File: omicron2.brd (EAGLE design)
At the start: 76.2 x 53.3 mm, 180 parts, among them IC1 XC6SLX4-2TQG144, IC2 TPS73033DBV, IC3 LD6806TD/12H, IC4 MT48LC64M4A2, IC5 M25P40-2253716, IC6 TPS73033DBV, X1 USB-MICRO-B-BOTTOM, X2 7C-33.3-1842039

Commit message: backup
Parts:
- removed C31, C32: (no value), rcl:C0603
- TP13, TP14, TP15, TP16: value TPTP15R -> TPTP20R; device testpad:TP15R -> testpad:TP20R
- moved TP10 55.7 mm to (71.1, 34.9), turned to 180 degrees
- moved C6 52.3 mm to (40.6, 50.2), turned to 270 degrees
- moved C2 48.0 mm to (40.6, 46.4)
- moved IC2 47.4 mm to (43.2, 48.3), turned to 180 degrees
- moved IC3 46.0 mm to (50.2, 48.3), turned to 180 degrees
- moved C1 44.5 mm to (45.7, 46.4), turned to 90 degrees
- moved C5 43.9 mm to (47.6, 46.4), turned to 90 degrees
- moved L3 41.8 mm to (41.3, 41.3)
- moved TP9 41.2 mm to (43.2, 43.8), turned to 0 degrees
- moved C33 39.9 mm to (36.8, 43.8), turned to 270 degrees
- moved X2 39.0 mm to (33.7, 43.8), turned to 270 degrees
- moved TP8 38.6 mm to (47.6, 43.8), turned to 0 degrees
- moved L2 34.6 mm to (43.2, 41.3), turned to 270 degrees
- moved L1 33.3 mm to (45.1, 41.3), turned to 270 degrees
- moved TP14 30.2 mm to (73.7, 49.5)
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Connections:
- net CLK_33: now also IC1.134; no longer IC1.51
- net GND: no longer C31.2, C32.2
- net LED1: now also IC1.48
- net LED2: now also IC1.47
- net LED3: now also IC1.46
- net M_A4: now also IC1.132; no longer IC1.101
- net M_PWREN: now also IC1.101
- net USB_D+: now also IC1.59; no longer C32.1, IC1.61
- net USB_D-: no longer C31.1
- net USB_PUP: now also IC1.67; no longer IC1.59
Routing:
- net +5V: track 26.3 -> 172.9 mm, vias 1 -> 3
- net GND: track 550.4 -> 671.7 mm, vias 50 -> 45
- net VCC_MEM: track 0.00 -> 50.4 mm, vias 0 -> 2
- net USB_S-: track 10.9 -> 52.2 mm, vias 0 -> 1
- net USB_S+: track 13.8 -> 52.1 mm, vias 0 -> 1
- net TDI: track 0.00 -> 35.8 mm, vias 0 -> 2
- net TCK: track 0.00 -> 34.7 mm, vias 0 -> 2
- net TMS: track 0.00 -> 31.6 mm, vias 0 -> 2
- net TDO: track 0.00 -> 30.8 mm, vias 0 -> 2
- net M_PWREN: track 0.00 -> 25.3 mm, vias 0 -> 1
- net M_A4: track 31.0 -> 52.1 mm
- net +3V3: track 220.3 -> 241.2 mm, vias 12 -> 14
- net CFG_DONE: track 2.17 -> 17.7 mm, vias 0 -> 2
- net FLASH_SO: track 23.9 -> 8.38 mm
- net LED1: track 0.00 -> 11.3 mm
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- added copper zone on layer 1, net GND
- added copper zone on layer 16, net GND
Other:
- board text added: "TCK"
- board text added: "TDI"
- board text added: "TMS"
- board text added: "omicron"
- board text added: "v2.0"

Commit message: backup
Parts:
- added C31, C32: 470nF, rcl:C0603
- added Q1, Q3: (no value), transistors:SOT323
- added Q2, Q4: BC807W, transistor-pnp:SOT323-BEC
- added R60, R61: 6k8 1%, rcl:R0603
- TP2: value TPTP15R -> TPTP20R; device testpad:TP15R -> testpad:TP20R
- moved TP2 54.9 mm to (73.7, 39.4)
- moved TP1 3.24 mm to (24.1, 12.1)
- moved C27 0.64 mm to (23.8, 28.3)
- moved C37 0.63 mm to (62.9, 34.9)
- moved L1 0.63 mm to (44.5, 41.3)
- moved L2 0.63 mm to (42.5, 41.3)
- moved L3 0.63 mm to (40.6, 41.3)
- moved TP3 0.63 mm to (60.3, 34.9)
- moved TP9 0.63 mm to (42.5, 43.8)
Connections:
- new net N$24: Q1.3, R60.2
- new net N$25: Q4.1, R61.1
- new net N$26: Q3.3, R61.2
- new net N$7: Q2.1, R60.1
- new net VIO33: IC1.44, Q3.1
- new net VIO50: IC1.45, Q1.1
- net +3V3: now also C31.1, C32.1, Q4.2
- net +5V: now also Q2.2
- net GND: now also C31.2, C32.2, Q1.2, Q3.2
- net S10: now also IC1.23; no longer IC1.24
- net S11: now also IC1.26; no longer IC1.27
- net S12: now also IC1.29; no longer IC1.30
- net S13: now also IC1.32; no longer IC1.33
- net S14: now also IC1.34; no longer IC1.39
- net S15: now also IC1.39; no longer IC1.41
- net S16: now also IC1.41; no longer IC1.44
- net S9: now also IC1.21; no longer IC1.22
- net SD10: now also IC1.24; no longer IC1.26
- net SD11: now also IC1.27; no longer IC1.29
- net SD12: now also IC1.30; no longer IC1.32
- net SD13: now also IC1.33; no longer IC1.34
- net SD14: now also IC1.35; no longer IC1.40
- net SD15: now also IC1.40; no longer IC1.43
- net SD16: now also IC1.43; no longer IC1.45
- net SD9: now also IC1.22; no longer IC1.23
- net VCC_B2: now also Q2.3, Q4.3
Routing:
- net VCC_B2: track 44.9 -> 60.3 mm, vias 1 -> 2
- net GND: track 671.7 -> 686.8 mm, vias 45 -> 44
- net VIO33: track 0.00 -> 14.5 mm, vias 0 -> 1
- net VIO50: track 0.00 -> 14.2 mm, vias 0 -> 1
- net +3V3: track 241.2 -> 253.4 mm, vias 14 -> 15
- net N$26: track 0.00 -> 3.77 mm
- net SD15: track 31.0 -> 28.2 mm
- net S16: track 25.8 -> 23.0 mm
- net +5V: track 172.9 -> 175.7 mm
- net SD16: track 35.1 -> 32.5 mm
- net SD14: track 26.5 -> 23.9 mm
- net N$24: track 0.00 -> 2.23 mm
- net S14: track 18.1 -> 16.2 mm
- net N$7: track 0.00 -> 1.82 mm
- net RESET_N: track 5.82 -> 7.61 mm
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- removed copper zone on layer 1, net GND
- removed copper zone on layer 16, net GND

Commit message: Initial commit.
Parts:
- added C38, C39: 470nF, rcl:C0603
- added C40: 2.2uF, rcl:C0603
- added R62, R63: 68, rcl:R0603
- added U$1: PIC10F320, pic10f320:SOT23
- moved LED1 48.4 mm to (26.0, 50.2), flipped to the bottom, turned to 0 degrees
- moved LED2 47.9 mm to (27.9, 50.2), flipped to the bottom, turned to 0 degrees
- moved LED4 47.9 mm to (31.8, 50.2), flipped to the bottom, turned to 0 degrees
- moved LED3 47.6 mm to (29.8, 50.2), flipped to the bottom, turned to 0 degrees
- moved R4 42.2 mm to (26.0, 47.0), flipped to the bottom, turned to 90 degrees
- moved R10 42.0 mm to (34.3, 47.6), flipped to the bottom, turned to 0 degrees
- moved R8 41.6 mm to (27.9, 47.0), flipped to the bottom, turned to 90 degrees
- moved R9 41.3 mm to (29.8, 47.0), flipped to the bottom, turned to 90 degrees
- moved LED5 15.4 mm to (46.4, 15.9), turned to 90 degrees
- moved R59 11.2 mm to (46.4, 14.0), turned to 0 degrees
- moved C4 8.82 mm to (37.5, 22.9), turned to 90 degrees
- moved C9 8.09 mm to (39.7, 26.0), turned to 0 degrees
- moved Q2 3.18 mm to (21.0, 2.54)
- moved Q4 3.18 mm to (18.4, 2.54)
- moved R60 2.54 mm to (22.2, 5.08)
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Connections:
- new net AD_RA0: IC1.46, U$1.1
- new net AD_RA1: IC1.47, U$1.3
- new net AD_RA3: IC1.51, U$1.6
- new net N$27: C39.1, R62.2, R63.2, U$1.4
- net +3V3: now also C38.1, U$1.5
- net +5V: now also C40.1
- net GND: now also C38.2, C39.2, C40.2, R62.1, U$1.2
- net LED1: now also IC1.139; no longer IC1.48
- net LED2: now also IC1.138; no longer IC1.47
- net LED3: now also IC1.133; no longer IC1.46
- net VCC_B2: now also R63.1
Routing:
- net N$27: track 0.00 -> 14.4 mm
- net CFG_DONE: track 17.7 -> 4.49 mm, vias 2 -> 0
- net AD_RA1: track 0.00 -> 12.8 mm
- net AD_RA3: track 0.00 -> 9.72 mm
- net AD_RA0: track 0.00 -> 9.60 mm
- net +3V3: track 253.4 -> 260.7 mm
- net GND: track 686.8 -> 690.4 mm, vias 44 -> 45
- net VCC_B2: track 60.3 -> 63.8 mm
- net N$25: track 1.67 -> 4.62 mm
- net N$4: track 1.58 -> 4.12 mm
- net N$26: track 3.77 -> 1.43 mm
- net LED2: track 10.7 -> 8.55 mm, vias 0 -> 1
- net LED1: track 11.3 -> 9.13 mm, vias 0 -> 1
- net N$91: track 1.58 -> 3.48 mm
- net +5V: track 175.7 -> 177.2 mm
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- added copper zone on layer 1, net GND
- added copper zone on layer 16, net GND

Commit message: Final touches.
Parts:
- added C41, C42, C43: 470nF, rcl:C0603
- moved TP9 0.64 mm to (42.5, 44.5)
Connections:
- net GND: now also C41.2, C42.2, C43.2
- net VCC_MEM: now also C41.1, C42.1, C43.1
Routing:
- net VCC_MEM: track 50.4 -> 62.2 mm
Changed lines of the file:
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@@
 <attribute name="TP_SIGNAL_NAME" value="" x="47.625" y="43.815" size="1.778" layer="28" rot="MR0" display="off"/>
 </element>
-<element name="TP9" library="testpad" package="TP15R" value="TPTP15R" x="42.545" y="43.815" rot="MR0">
-<attribute name="TP_SIGNAL_NAME" value="" x="42.545" y="43.815" size="1.778" layer="28" rot="MR0" display="off"/>
+<element name="TP9" library="testpad" package="TP15R" value="TPTP15R" x="42.545" y="44.45" rot="MR0">
+<attribute name="TP_SIGNAL_NAME" value="" x="42.545" y="44.45" size="1.778" layer="28" rot="MR0" display="off"/>
 </element>
 <element name="TP10" library="testpad" package="TP15R" value="TPTP15R" x="71.12" y="34.925" rot="MR180">
@@
 <element name="C39" library="rcl" package="C0603" value="470nF" x="36.83" y="3.81"/>
 <element name="C40" library="rcl" package="C0603" value="2.2uF" x="66.675" y="34.925" rot="MR0"/>
+<element name="C41" library="rcl" package="C0603" value="470nF" x="57.785" y="31.115" rot="MR270"/>
+<element name="C42" library="rcl" package="C0603" value="470nF" x="55.245" y="35.56" rot="MR90"/>
+<element name="C43" library="rcl" package="C0603" value="470nF" x="50.8" y="32.385" rot="MR0"/>
 </elements>
 <signals>
@@
 <wire x1="26.935" y1="3.16" x2="28.56" y2="3.16" width="0.254" layer="16"/>
 <wire x1="28.56" y1="3.16" x2="29.845" y2="4.445" width="0.254" layer="16"/>
+<contactref element="C43" pad="2"/>
+<contactref element="C42" pad="2"/>
+<contactref element="C41" pad="2"/>
 </signal>
 <signal name="VCCINT">
@@
 <wire x1="42.23" y1="45.505" x2="40.64" y2="45.505" width="0.254" layer="16"/>
 <wire x1="42.545" y1="42.225" x2="40.64" y2="42.225" width="0.254" layer="16"/>
-<wire x1="42.545" y1="42.225" x2="42.545" y2="43.815" width="0.254" layer="16"/>
-<wire x1="42.545" y1="43.815" x2="42.545" y2="45.19" width="0.254" layer="16"/>
+<wire x1="42.545" y1="42.225" x2="42.545" y2="44.45" width="0.254" layer="16"/>
+<wire x1="42.545" y1="44.45" x2="42.545" y2="45.19" width="0.254" layer="16"/>
 <wire x1="42.545" y1="45.19" x2="42.23" y2="45.505" width="0.254" layer="16"/>
 </signal>
@@
 <via x="58.42" y="36.195" extent="1-16" drill="0.5"/>
 <wire x1="55.245" y1="36.195" x2="58.42" y2="36.195" width="0.254" layer="1"/>
+<contactref element="C41" pad="1"/>
+<contactref element="C42" pad="1"/>
+<contactref element="C43" pad="1"/>
+<wire x1="57.785" y1="31.965" x2="57.785" y2="33.335" width="0.254" layer="16"/>
+<wire x1="57.785" y1="33.335" x2="60.325" y2="33.335" width="0.254" layer="16"/>
+<wire x1="55.245" y1="34.71" x2="55.245" y2="33.335" width="0.254" layer="16"/>
+<wire x1="55.245" y1="33.335" x2="57.785" y2="33.335" width="0.254" layer="16"/>
+<wire x1="51.65" y1="32.385" x2="54.295" y2="32.385" width="0.254" layer="16"/>
+<wire x1="54.295" y1="32.385" x2="55.245" y2="33.335" width="0.254" layer="16"/>
 </signal>
 <signal name="N$7">

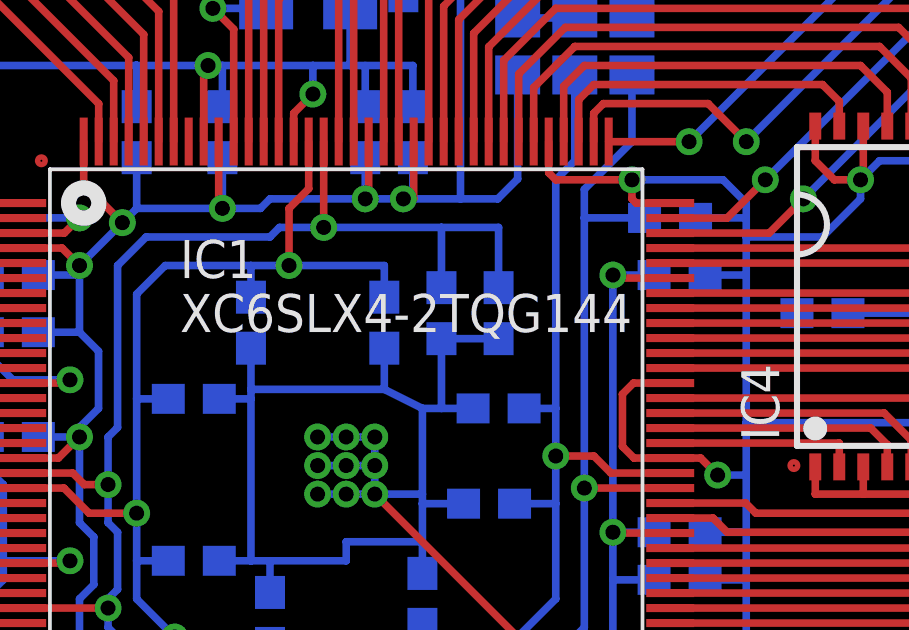
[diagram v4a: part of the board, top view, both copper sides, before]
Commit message: v2.0 component values
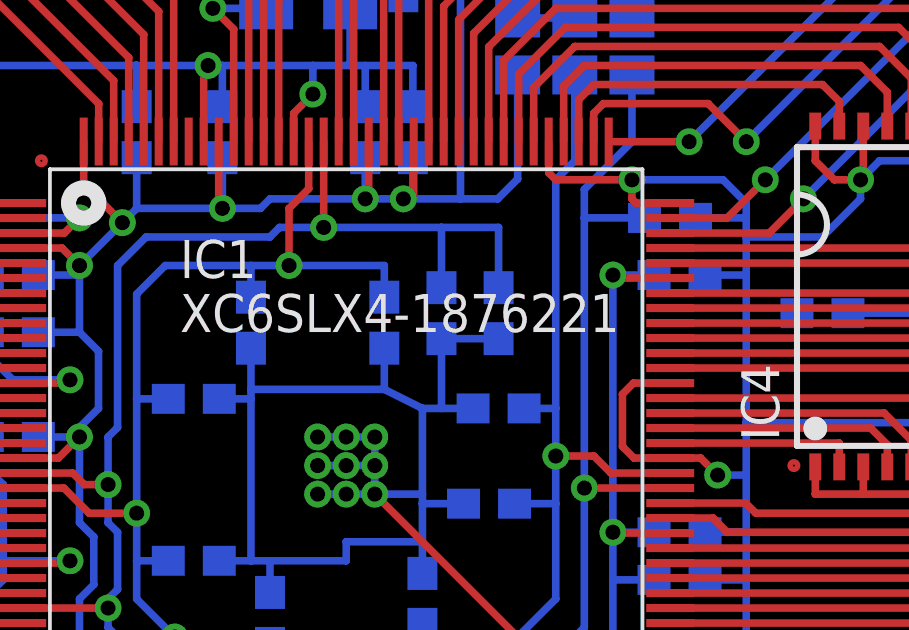
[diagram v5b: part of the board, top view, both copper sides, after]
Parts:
- C1, C36: value 10uF -> 10nF
- C34, C35: value (none) -> 470nF
- C39: value 470nF -> 10nF
- C5: value 1uF -> 2.2uF
- IC1: value XC6SLX4-2TQG144 -> XC6SLX4-1876221
- IC2, IC6: value TPS73033DBV -> TPS73033DBV-1135395
- IC3: value LD6806TD/12H -> LD6806TD/12H-2095494
- IC4: value MT48LC64M4A2 -> H57V2562GTR-75C-1907383
- L1, L2, L3: value (none) -> 100nH
- LED5: value RED -> RED-2099221
- Q1, Q3: value (none) -> PDTC123-1757992
- R1, R2: value 27 -> 27 1%
- R11, R12, R13, R14, R15, R16, R17, R18, R19, R20, R21, R22, R23, R24, R25, R26: value (none) -> 68
- R27, R28, R29, R30, R31, R32, R33, R34, R35, R36, R37, R38, R39, R40, R41, R42, R43, R44, R45, R46, R47, R48, R49, R50, R51, R52, R53, R54, R55, R56, R57, R58: value (none) -> 330k
- R5, R7: value 47k -> 330k
- R62: value 68 -> 6k8 1%
- R63: value 68 -> 4k7 1%
- U$1: value PIC10F320 -> PIC10F320-2074912
